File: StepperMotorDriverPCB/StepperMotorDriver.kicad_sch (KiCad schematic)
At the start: 57 parts, among them IC2 TMC2209-LA, J1 Conn_01x02_Pin, J2 Conn_01x01_Pin, J3 Conn_01x01_Pin, J4 Conn_01x04_Socket, J5 USB_C_Receptacle_USB2.0_14P, J6 Conn_01x04_Pin, J7 Conn_01x02_Pin, J8 Conn_01x01_Pin, J9 Conn_01x01_Pin, SW1 SW_SPDT, U2 SN65HVD232, U3 STM32F423CHU6, U5 TSR1-2433E, U6 MT6701CT, Y2 16MHz

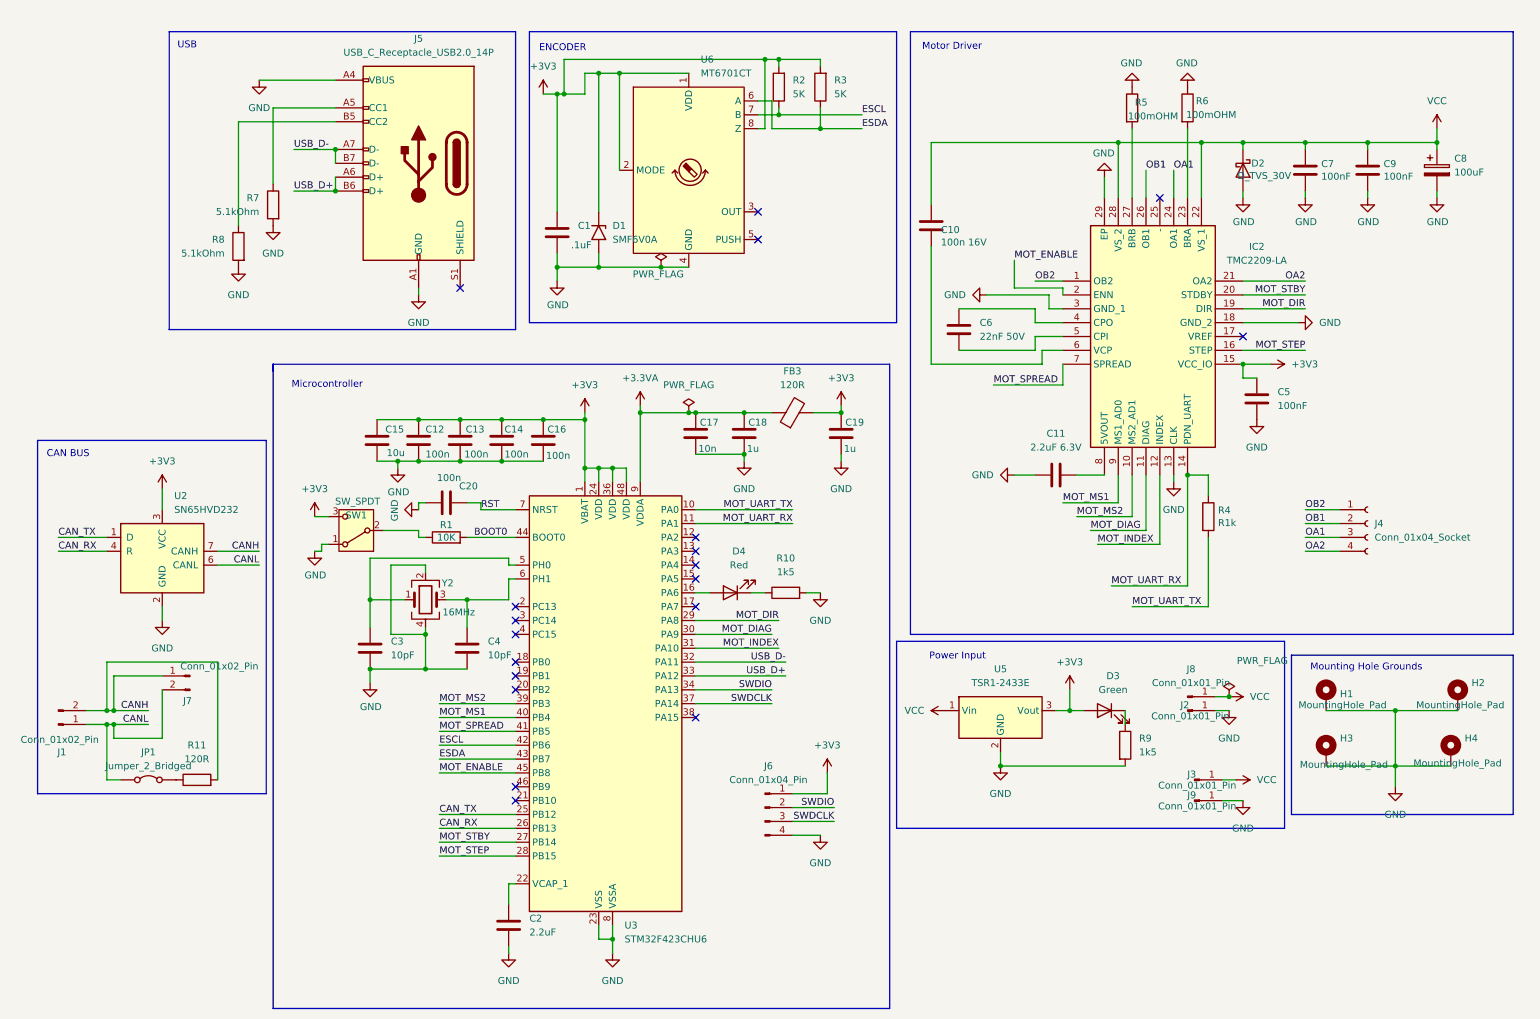
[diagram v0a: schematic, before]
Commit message: Replaced Microcontrollers and Power Distribution System
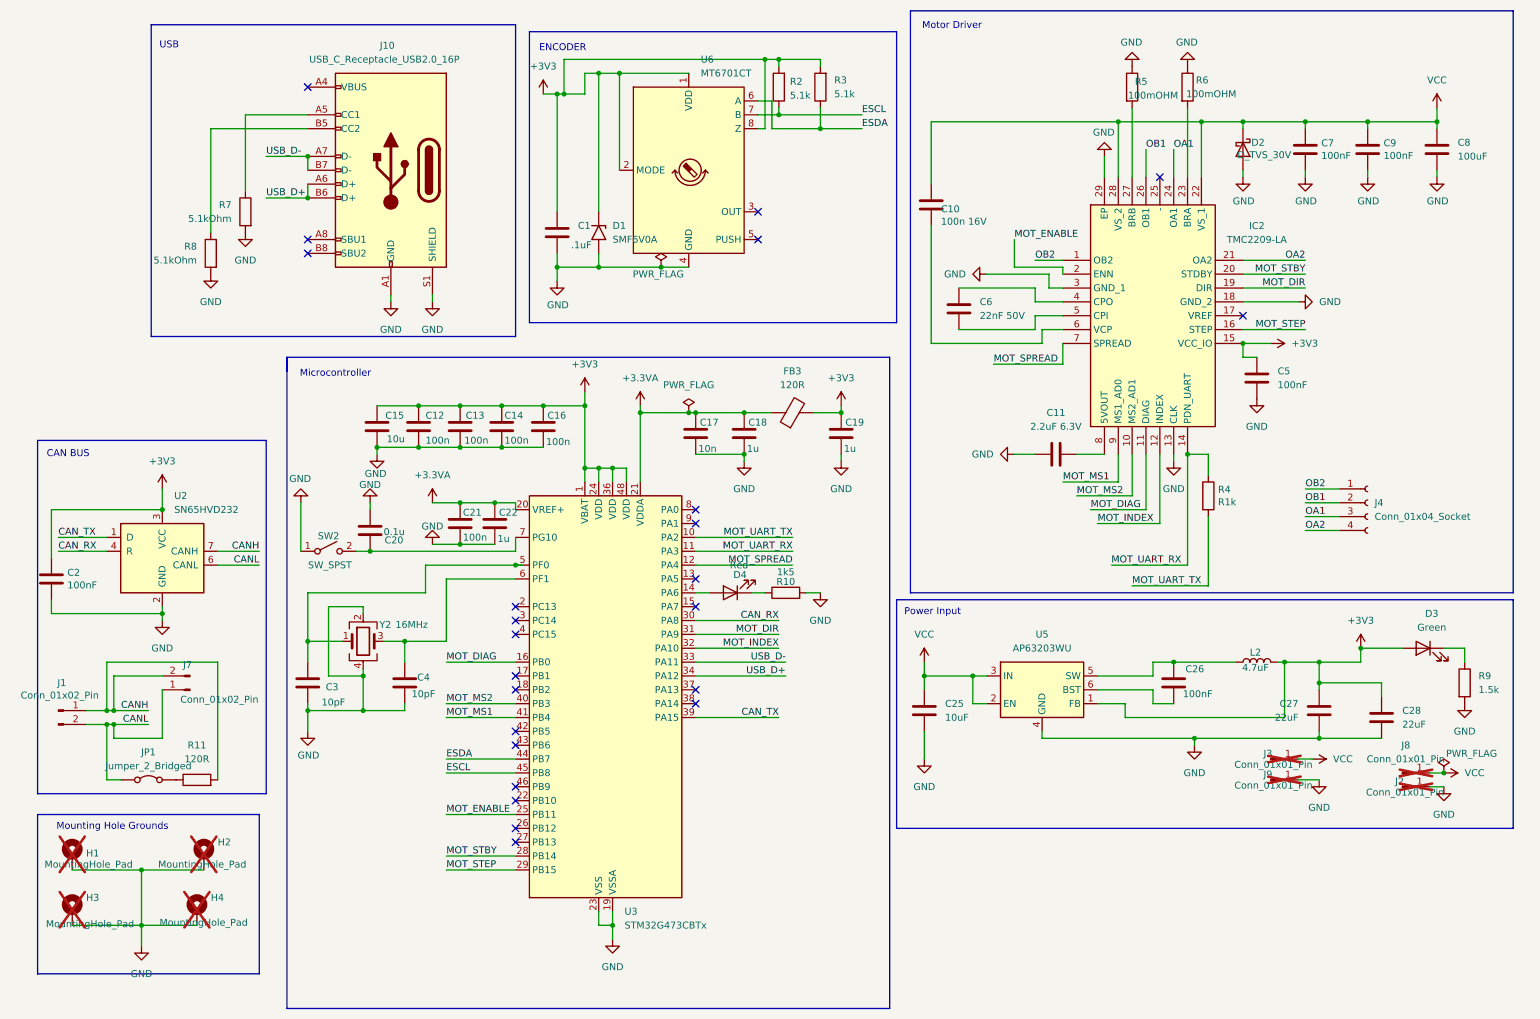
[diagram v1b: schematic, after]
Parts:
- removed J5: USB_C_Receptacle_USB2.0_14P, Connector_USB:USB_C_Receptacle_GCT_USB4125-xx-x-0190_6P_TopMnt_Horizontal, symbol Connector:USB_C_Receptacle_USB2.0_14P
- removed J6: Conn_01x04_Pin, Connector_PinHeader_2.54mm:PinHeader_1x04_P2.54mm_Vertical, symbol Connector:Conn_01x04_Pin
- removed R1: 10K, Resistor_SMD:R_0402_1005Metric, symbol Device:R
- removed SW1: SW_SPDT, Button_Switch_SMD:SW_SPST_B3U-1100P-B, symbol Switch:SW_SPDT
- removed U3: STM32F423CHU6, Package_DFN_QFN:QFN-48-1EP_7x7mm_P0.5mm_EP5.6x5.6mm, symbol MCU_ST_STM32F4:STM32F423CHUx
- removed U5: TSR1-2433E, Converter_DCDC:Converter_DCDC_TRACO_TSR1-xxxxE_THT, symbol Regulator_Switching:TSR1-2433E
- added C21: 100n, Capacitor_SMD:C_0402_1005Metric, symbol Device:C
- added C22: 1u, Capacitor_SMD:C_0402_1005Metric, symbol Device:C
- added C25: 10uF, Capacitor_SMD:C_0603_1608Metric, symbol Device:C
- added C26: 100nF, Capacitor_SMD:C_0402_1005Metric, symbol Device:C
- added C27, C28: 22uF, Capacitor_SMD:C_0603_1608Metric, symbol Device:C
- added J10: USB_C_Receptacle_USB2.0_16P, Connector_USB:USB_C_Receptacle_Palconn_UTC16-G, symbol Connector:USB_C_Receptacle_USB2.0_16P
- added L2: 4.7uF, Inductor_SMD:L_Chilisin_BMRA00050530, symbol Device:L
- added SW2: SW_SPST, Button_Switch_THT:SW_PUSH_1P1T_6x3.5mm_H5.0_APEM_MJTP1250, symbol Switch:SW_SPST
- added U3: STM32G473CBTx, Package_QFP:LQFP-48_7x7mm_P0.5mm, symbol MCU_ST_STM32G4:STM32G473CBTx
- added U5: AP63203WU, Package_TO_SOT_SMD:TSOT-23-6, symbol Regulator_Switching:AP63203WU
- C10: footprint Capacitor_SMD:C_0504_1310Metric -> Capacitor_SMD:C_0603_1608Metric
- C2: value 2.2uF -> 100nF; footprint Capacitor_SMD:C_0603_1608Metric -> Capacitor_SMD:C_0402_1005Metric; LCSC (none) -> C13585
- C20: value 100n -> 0.1u
- C8: footprint Capacitor_SMD:CP_Elec_6.3x4.5 -> Capacitor_SMD:C_0603_1608Metric; symbol Device:C_Polarized -> Device:C
- D2: footprint Diode_SMD:D_SOD-123 -> Diode_SMD:D_0603_1608Metric
- H1, H2, H3, H4: now not fitted
- J1, J7: footprint Connector_Molex:Molex_MicroClasp_55932-0210_1x02_P2.00mm_Vertical -> Connector_JST:JST_XH_S2B-XH-A-1_1x02_P2.50mm_Horizontal
- J2, J3, J8, J9: footprint Connector_Wire:SolderWirePad_1x01_SMD_1x2mm -> TestPoint:TestPoint_Pad_4.0x4.0mm; now not fitted
- J4: footprint TerminalBlock:TerminalBlock_Altech_AK300-4_P5.00mm -> Connector_JST:JST_XH_S4B-XH-A-1_1x04_P2.50mm_Horizontal
- JP1: footprint TestPoint:TestPoint_2Pads_Pitch2.54mm_Drill0.8mm -> Jumper:SolderJumper-2_P1.3mm_Open_RoundedPad1.0x1.5mm
- R2, R3: value 5K -> 5.1k
- R9: value 1k5 -> 1.5k
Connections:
- net RST is gone; now on net GND: C20.2
- net +3.3VA: now also C21.1, C22.1, U3.20 (VREF+), U3.21 (VDDA)
- net +3V3: now also C2.1, C27.1, C28.2, L2.2, U3.1 (VBAT), U3.24 (VDD), U3.36 (VDD), U3.48 (VDD), U5.1 (FB)
- net CANH: now also J1.1 (Pin_1), J7.2 (Pin_2); no longer J1.2 (Pin_2), J7.1 (Pin_1)
- net CANL: now also J1.2 (Pin_2), J7.1 (Pin_1); no longer J1.1 (Pin_1), J7.2 (Pin_2)
- net CAN_RX: now also U3.30 (PA8)
- net CAN_TX: now also U3.39 (PA15)
- net ESCL: now also U3.45 (PB8)
- net ESDA: now also U3.44 (PB7)
- net GND: now also C21.2, C22.2, C25.1, C27.2, C28.1, J10.A1 (GND), J10.A12 (GND), J10.B1 (GND), J10.B12 (GND), J10.S1 (SHIELD), SW2.1 (A), U3.19 (VSSA), U3.23 (VSS), U3.35 (VSS), U3.47 (VSS), U5.4 (GND); no longer C20.1
- net MOT_DIAG: now also U3.16 (PB0)
- net MOT_DIR: now also U3.31 (PA9)
- net MOT_ENABLE: now also U3.25 (PB11)
- net MOT_INDEX: now also U3.32 (PA10)
- net MOT_MS1: now also U3.41 (PB4)
- net MOT_MS2: now also U3.40 (PB3)
- net MOT_SPREAD: now also U3.12 (PA4)
- net MOT_STBY: now also U3.28 (PB14)
- net MOT_STEP: now also U3.29 (PB15)
- net MOT_UART_RX: now also U3.11 (PA3)
- net MOT_UART_TX: now also U3.10 (PA2)
- net USB_D+: now also J10.A6 (D+), J10.B6 (D+), U3.34 (PA12)
- net USB_D-: now also J10.A7 (D-), J10.B7 (D-), U3.33 (PA11)
- net VCC: now also C25.2, U5.2 (EN), U5.3 (IN)
- net at C3.1, Y2.1: now also U3.5 (PF0)
- net at C4.1, Y2.3: now also U3.6 (PF1)
- net at R7.1: now also J10.A5 (CC1)
- net at R8.1: now also J10.B5 (CC2)
- net at D4.2 (A): now also U3.14 (PA6)
- new net: C20.1, SW2.2 (B), U3.7 (PG10)
- new net: C26.1, L2.1, U5.5 (SW)
- new net: C26.2, U5.6 (BST)
- new net: J10.A4 (VBUS), J10.A9 (VBUS), J10.B4 (VBUS), J10.B9 (VBUS)
- no-connect marks 19 -> 24
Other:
- moved on the sheet: C10, C11, C12, C13, C14, C15, C16, C3, C4, C5, C6, C7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

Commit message: Major changes to layout
Made everything but encoder on top layer. Changed to stronger MC, new buttons, etc.
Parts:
- removed C8: 100uF, Capacitor_SMD:C_0603_1608Metric, symbol Device:C
- added C8: 100uF, Capacitor_SMD:CP_Elec_3x5.3, symbol Device:C_Polarized
- C27, C28: footprint Capacitor_SMD:C_0603_1608Metric -> Capacitor_SMD:C_0805_2012Metric
- H1, H2, H3, H4: now fitted
- R5, R6: footprint Resistor_SMD:R_0402_1005Metric -> Resistor_SMD:R_1206_3216Metric
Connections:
- net CANH: now also J7.1 (Pin_1); no longer J7.2 (Pin_2)
- net CANL: now also J7.2 (Pin_2); no longer J7.1 (Pin_1)
- net GND: now also C20.1, C8.2; no longer C20.2
- net VCC: now also C8.1
- net at SW2.2 (B), U3.7 (PG10): now also C20.2; no longer C20.1
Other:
- moved on the sheet: C20, C21, C22, J7, R2, R3

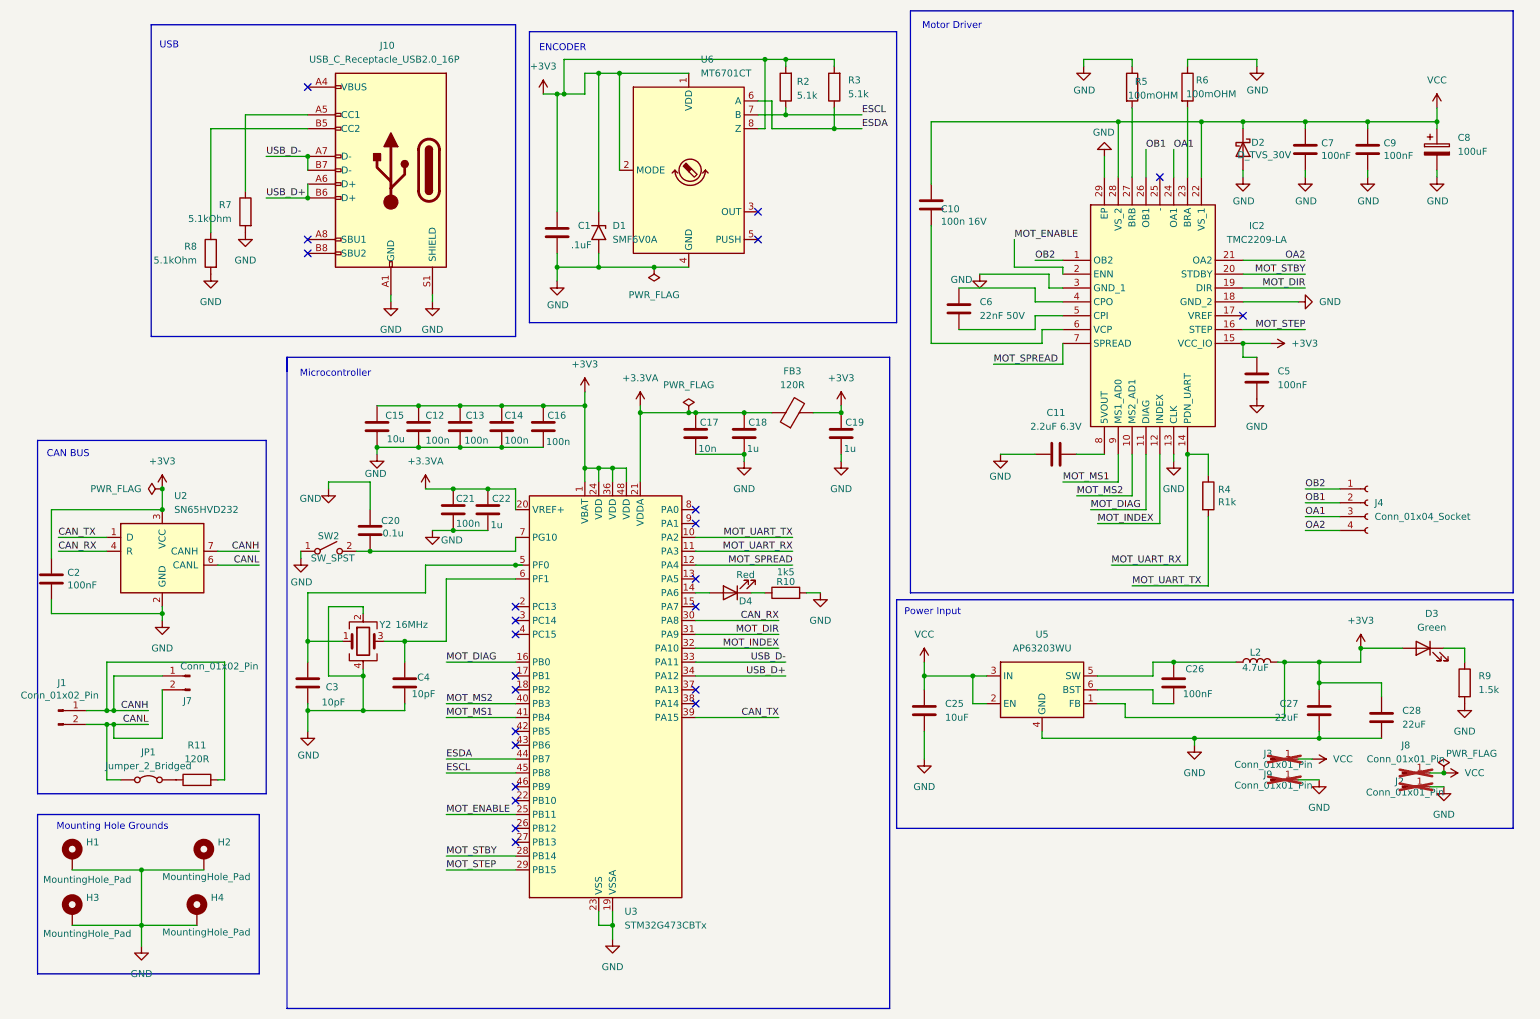
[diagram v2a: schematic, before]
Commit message: Major Structural Updates.
Updated mounting hardware and PD
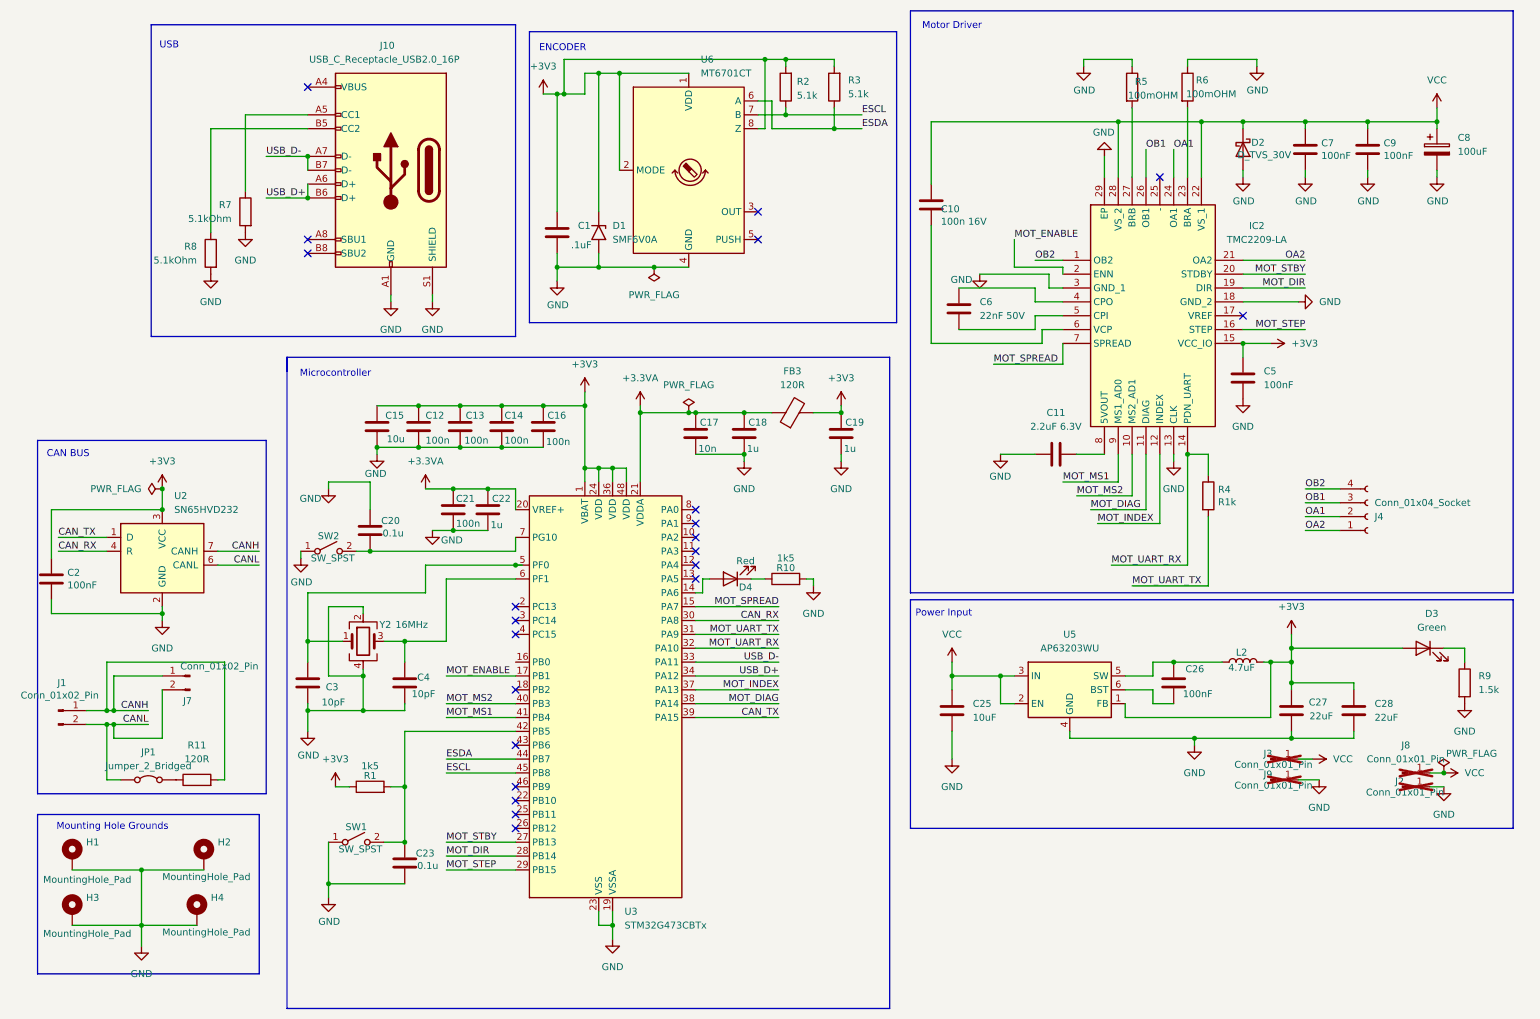
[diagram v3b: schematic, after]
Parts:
- added C23: 0.1u, Capacitor_SMD:C_0402_1005Metric, symbol Device:C
- added R1: 1k5, Resistor_SMD:R_0402_1005Metric, symbol Device:R
- added SW1: SW_SPST, Button_Switch_THT:SW_PUSH_1P1T_6x3.5mm_H5.0_APEM_MJTP1250, symbol Switch:SW_SPST
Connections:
- net +3V3: now also R1.1
- net GND: now also C23.2, SW1.1 (A)
- net MOT_DIAG: now also U3.38 (PA14); no longer U3.16 (PB0)
- net MOT_DIR: now also U3.28 (PB14); no longer U3.31 (PA9)
- net MOT_ENABLE: now also U3.17 (PB1); no longer U3.25 (PB11)
- net MOT_INDEX: now also U3.37 (PA13); no longer U3.32 (PA10)
- net MOT_SPREAD: now also U3.15 (PA7); no longer U3.12 (PA4)
- net MOT_STBY: now also U3.27 (PB13); no longer U3.28 (PB14)
- net MOT_UART_RX: now also U3.32 (PA10); no longer U3.11 (PA3)
- net MOT_UART_TX: now also U3.31 (PA9); no longer U3.10 (PA2)
- net OA1: now also J4.2 (Pin_2); no longer J4.3 (Pin_3)
- net OA2: now also J4.1 (Pin_1); no longer J4.4 (Pin_4)
- net OB1: now also J4.3 (Pin_3); no longer J4.2 (Pin_2)
- net OB2: now also J4.4 (Pin_4); no longer J4.1 (Pin_1)
- net at U3.42 (PB5): now also C23.1, R1.2, SW1.2 (B)
- no-connect marks 24 -> 22
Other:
- moved on the sheet: C25, C27, C28, C5, D4, L2, R10, U5

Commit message: Updates to circuitry
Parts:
- added J5: Conn_01x02_Pin, Connector_PinHeader_2.00mm:PinHeader_1x02_P2.00mm_Vertical, symbol Connector:Conn_01x02_Pin
- added JP2: Jumper_2_Bridged, Jumper:SolderJumper-2_P1.3mm_Open_RoundedPad1.0x1.5mm, symbol Jumper:Jumper_2_Bridged
- added R12: 10k, Resistor_SMD:R_0402_1005Metric, symbol Device:R
- C8: footprint Capacitor_SMD:CP_Elec_3x5.3 -> Capacitor_THT:CP_Radial_D5.0mm_P2.50mm
- J2, J3, J8, J9: footprint TestPoint:TestPoint_Pad_4.0x4.0mm -> TestPoint:TestPoint_Plated_Hole_D2.0mm; now fitted
- R1: value 1k5 -> 10k
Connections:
- net +3V3: now also JP2.1 (A)
- net CAN_TX: now also U3.41 (PB4); no longer U3.39 (PA15)
- net ESCL: now also U3.39 (PA15); no longer U3.45 (PB8)
- net GND: now also R12.1
- net MOT_DIAG: now also U3.42 (PB5); no longer U3.38 (PA14)
- net MOT_DIR: now also U3.26 (PB12); no longer U3.28 (PB14)
- net MOT_INDEX: now also U3.40 (PB3); no longer U3.37 (PA13)
- net MOT_MS1: now also U3.46 (PB9); no longer U3.41 (PB4)
- net MOT_MS2: now also U3.43 (PB6); no longer U3.40 (PB3)
- net MOT_STBY: now also U3.25 (PB11); no longer U3.27 (PB13)
- net at U3.2 (PC13): now also C23.1, R1.2, SW1.2 (B)
- new net: JP2.2 (B), R12.2, U3.45 (PB8)
- new net SWCLK: J5.1 (Pin_1), U3.38 (PA14)
- new net SWDIO: J5.2 (Pin_2), U3.37 (PA13)
- no-connect marks 22 -> 20
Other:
- moved on the sheet: C23, R1, SW1
